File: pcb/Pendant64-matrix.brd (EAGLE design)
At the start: 50.5 x 42.5 mm, 84 parts, among them U2 MMA8653FC

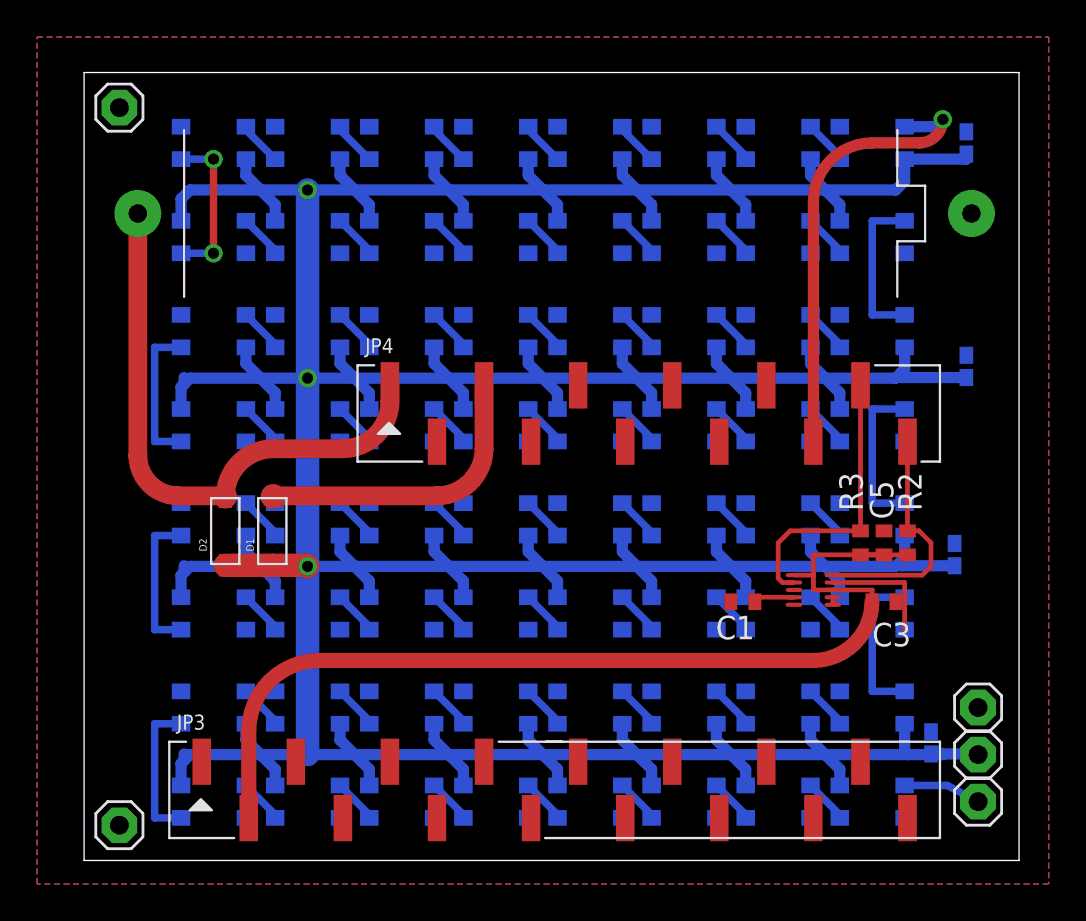
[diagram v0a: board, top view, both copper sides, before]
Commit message: added a second AAA battery, relocated wifi to center of board
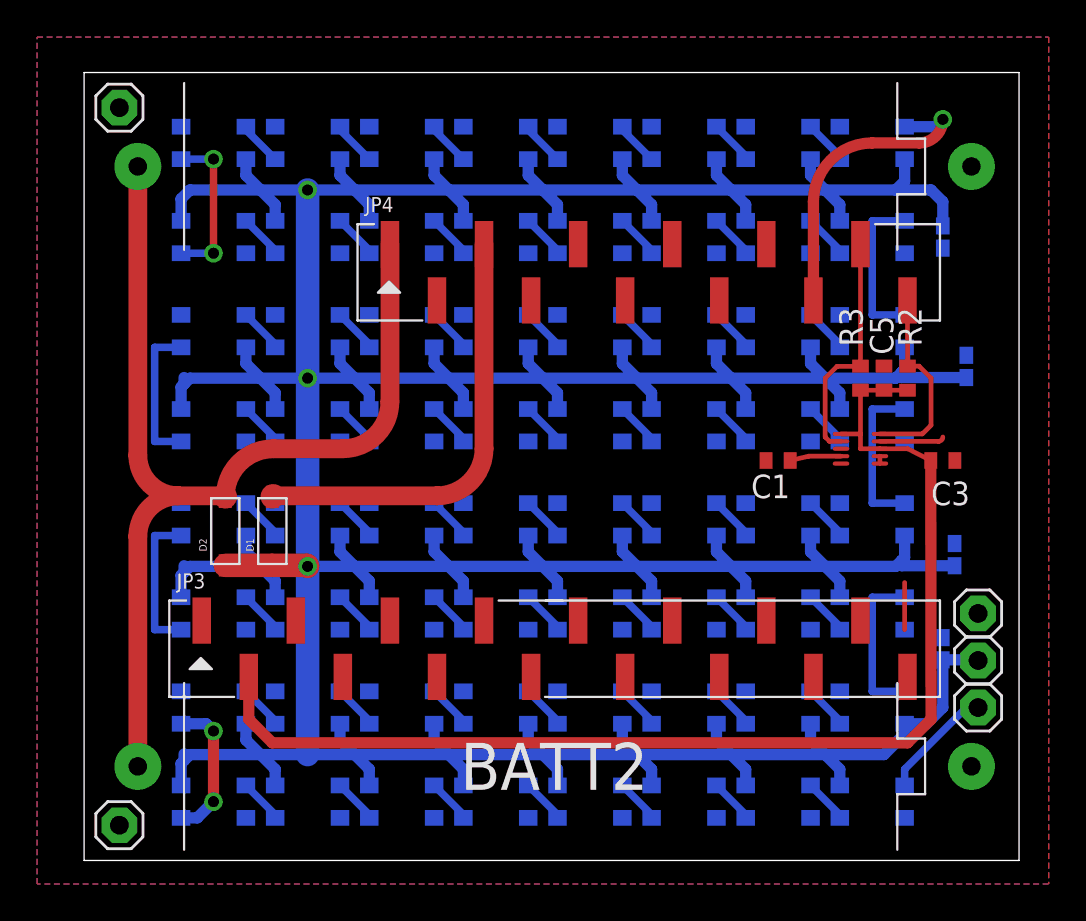
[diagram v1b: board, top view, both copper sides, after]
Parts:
- added BATT2: AAA, adafruit:12BH412
- moved C5 8.89 mm to (43.2, 26.0)
- moved R2 8.89 mm to (44.5, 26.0)
- moved R3 8.89 mm to (41.9, 26.0)
- moved C3 8.25 mm to (46.4, 21.6)
- moved U2 8.03 mm to (41.9, 22.2)
- moved C1 7.85 mm to (37.5, 21.6)
- moved JP4 7.62 mm to (30.5, 31.8)
- moved JP3 7.62 mm to (25.4, 11.4)
- moved C8 5.24 mm to (46.4, 33.7), turned to 270 degrees
- moved C2 5.12 mm to (46.4, 11.4)
- moved JP1 5.08 mm to (48.3, 8.26)
- moved JP2 5.08 mm to (48.3, 13.3)
- moved JP5 5.08 mm to (48.3, 10.8)
- moved BATT1 2.54 mm to (25.4, 37.5)
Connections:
- net GND: now also BATT2.+
- net VBAT: now also BATT2.-
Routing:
- net VBAT: track 30.6 -> 56.3 mm
- net +3V3: track 54.3 -> 64.8 mm
- net VUSB: track 15.9 -> 23.5 mm
- net LED_DIN: track 24.0 -> 16.4 mm
- net SDA: track 13.1 -> 10.6 mm
- net SCL: track 15.4 -> 12.9 mm
- net LED_DOUT: track 4.18 -> 6.22 mm
- net VDD: track 331.0 -> 332.4 mm
- net N$62: track 2.21 -> 2.77 mm
- net N$65: track 7.93 -> 7.84 mm, vias 0 -> 2
